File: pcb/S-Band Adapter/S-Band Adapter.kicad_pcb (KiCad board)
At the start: 2 copper layers, 94 x 61 mm, 9 parts, among them J1 CT3151SP-2, J2 FTSH-107-01-L-DV-K-A, J3 ERF8-030-05.0-L-DV-TR, J4 532611071, J5 CT3151SP-2

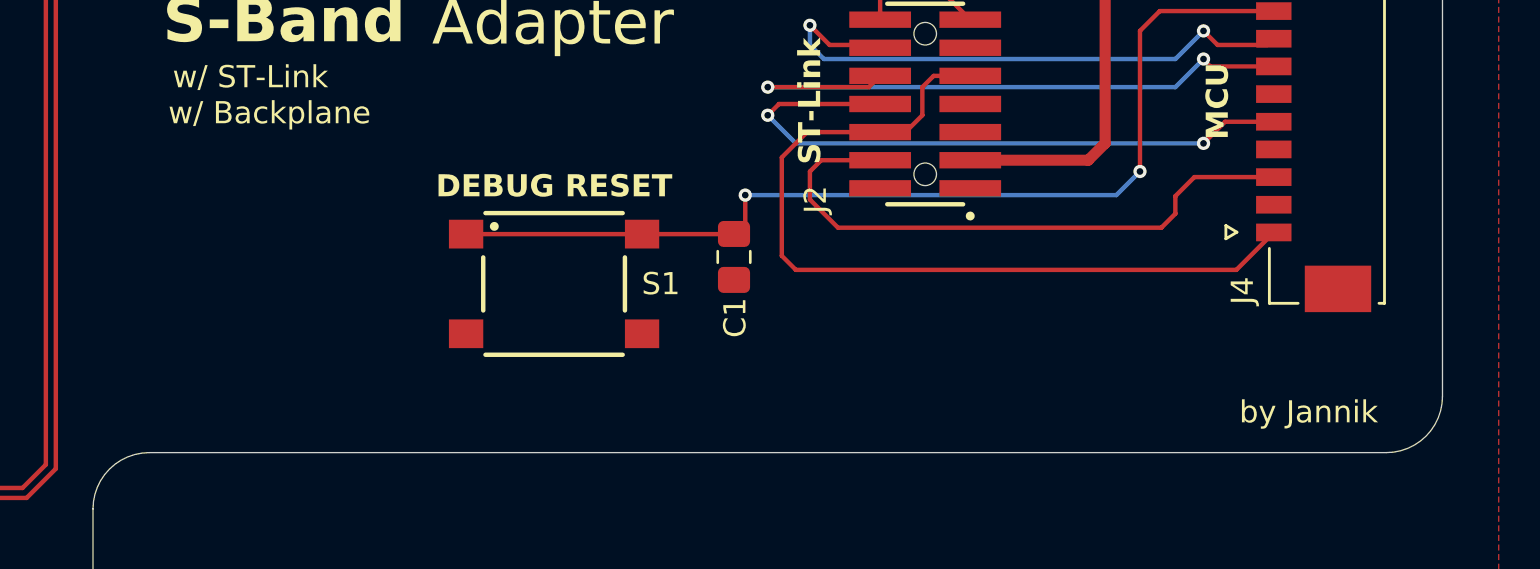
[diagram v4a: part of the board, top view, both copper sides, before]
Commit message: Added aisler logo
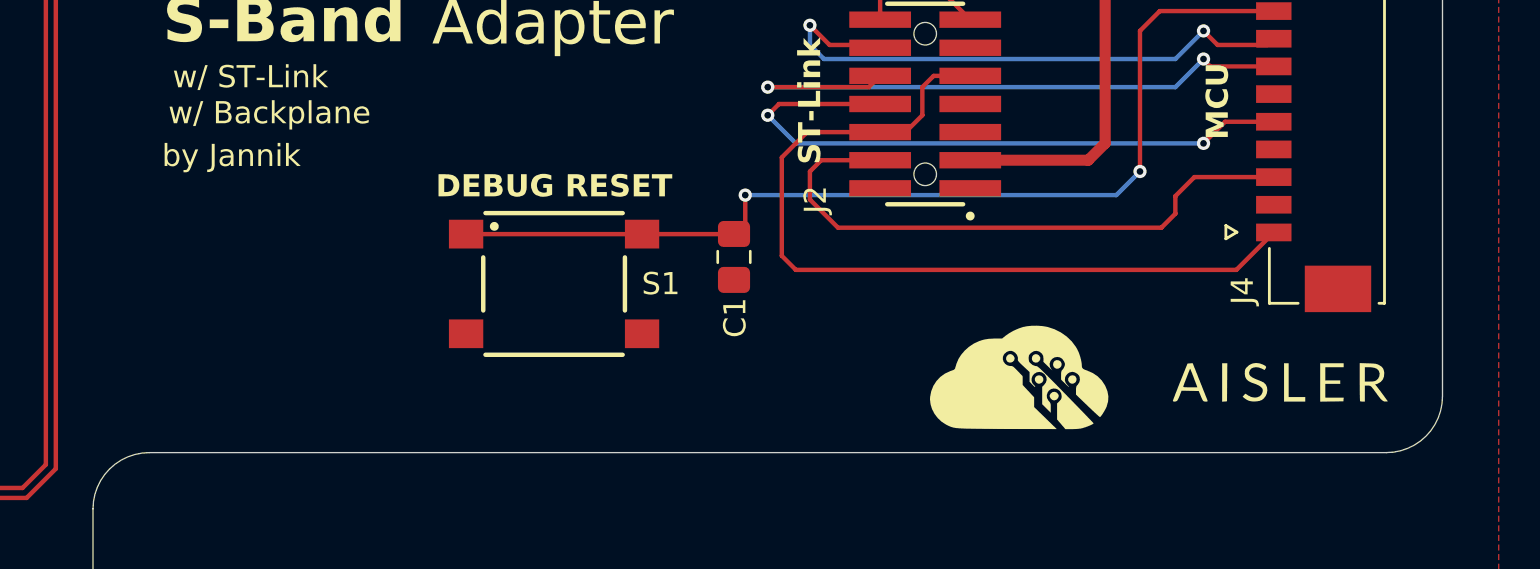
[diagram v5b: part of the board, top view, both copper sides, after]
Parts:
- added G***: LOGO, LOGO, F.Cu at (236.3, 95.9)
